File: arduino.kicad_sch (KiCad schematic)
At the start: 11 parts, among them J4 Conn_01x01_Female, J5 Conn_01x01_Female, U10 74HC4051, U11 74HC4051, U9 LM358

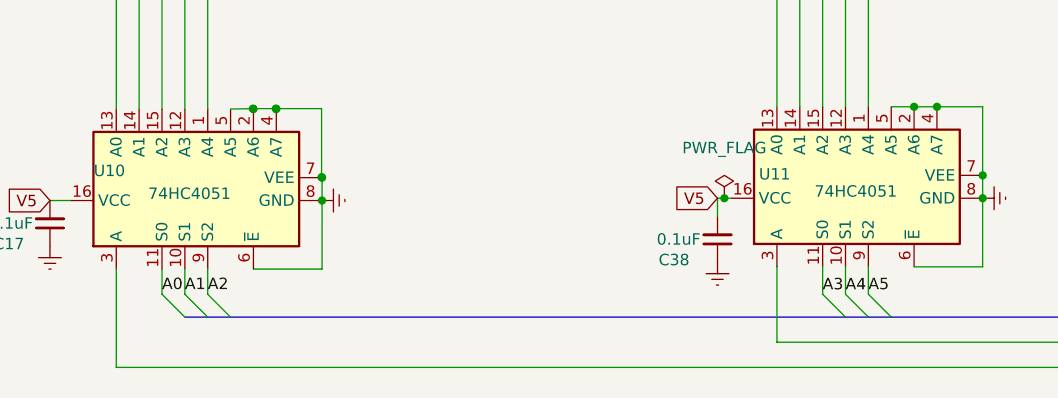
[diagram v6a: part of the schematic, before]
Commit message: mux and opamp layouts completed and new ext conn to display
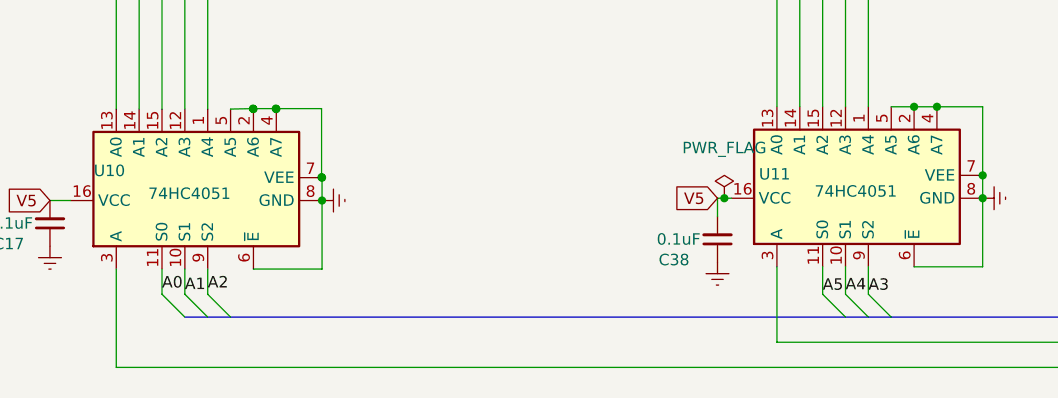
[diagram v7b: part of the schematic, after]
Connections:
- net A3: now also U11.9 (S2); no longer U11.11 (S0)
- net A5: now also U11.11 (S0); no longer U11.9 (S2)
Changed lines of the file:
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@@
     (effects (font (size 1.27 1.27)) (justify left bottom))
   )
-  (label "A3" (at 210.058 148.2852 0)
+  (label "A3" (at 215.138 148.336 0)
     (effects (font (size 1.27 1.27)) (justify left bottom))
   )
@@
     (effects (font (size 1.27 1.27)) (justify left bottom))
   )
-  (label "A0" (at 136.652 148.2598 0)
+  (label "A0" (at 136.652 148.082 0)
     (effects (font (size 1.27 1.27)) (justify left bottom))
   )
@@
     (effects (font (size 1.27 1.27)) (justify left bottom))
   )
-  (label "A2" (at 141.732 148.2598 0)
+  (label "A2" (at 141.732 148.082 0)
     (effects (font (size 1.27 1.27)) (justify left bottom))
   )
@@
     (effects (font (size 1.27 1.27)) (justify left bottom))
   )
-  (label "A5" (at 215.138 148.2729 0)
+  (label "A5" (at 210.058 148.336 0)
     (effects (font (size 1.27 1.27)) (justify left bottom))
   )
